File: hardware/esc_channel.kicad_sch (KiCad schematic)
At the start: 39 parts, among them Q3 DOY180N03T, Q4 DOY180N03T, Q5 DOY180N03T, Q6 DOY180N03T, Q7 DOY180N03T, Q8 DOY180N03T, U13 AT32F421G8U7, U14 NSG2065Q

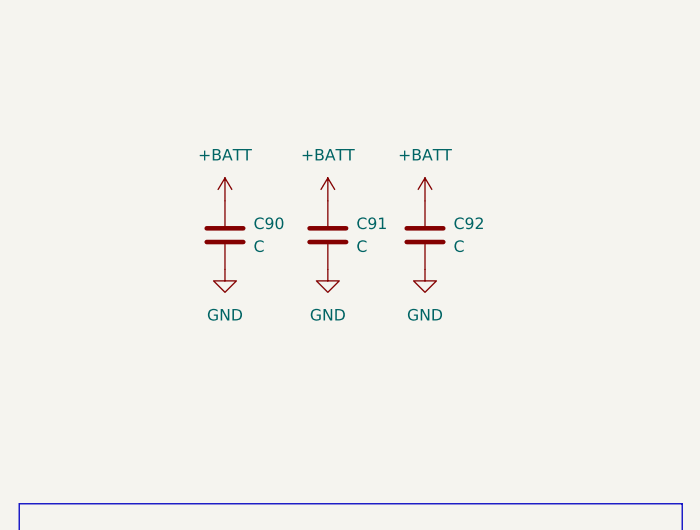
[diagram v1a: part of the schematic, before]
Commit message: Circuit: B3 bulk caps and ESP32-C3FH4, LDO caps, BMI270 aux pins, BOOTSEL 1k, unused pads
CIRCUIT_REVIEW B3, S2, S4, S5 and decision D9; LAYOUT_REVIEW 5.3 (pure
clean-up). Values and parts from hardware/KiCad-Library/PARTS-USED.md.

- B3: the 16 +BATT bulk caps had value "C" and no part. C90-C103 (0805)
  4.7uF 50V X5R CL21A475KBQNNNE (C98192, already C18/C19); C105/C106 (1206)
  4.7uF 50V X7R TCC1206X7R475K500HT (C380366, OpenESC).
- D9/B3: U22 is ESP32-C3FH4 (C2858491, in-package flash), as its NC SPI pins
  require; its in-package-flash pads 19, 21-24 deleted per instance (20 was
  already gone). L4 MPN MLZ2012M150WT000 (TDK, SX1281 reference BOM, LCSC not
  in the catalogue); D9 MPN/manufacturer/LCSC from the catalogue.
- S2, LP5912 windows (CIN > 0.5 uF effective, COUT 0.7-10 uF): U7 COUT C28
  22uF -> 1uF CL05A105KA5NQNC; U6 COUT C27 22uF -> 4.7uF CL05A475MP5NRNC;
  U7 CIN C26 100nF -> 1uF GRM033R61A105ME44D in the existing 0201 (an 0402
  does not fit beside U7 without moving parts; ~0.5 uF effective at 4.6 V,
  so it is marginal until U7 moves to the Core in R2, decision S1).
- S4: BMI270 U8 ASDx/ASCx (pins 2/3) were on GND, which the datasheet
  forbids; now +3.3V (VDDIO), valid for the LSM6DSV16X option too.
  Schematic: the GND drop replaced by a +3.3V symbol. Core: pads 2/3 and the
  via between them re-netted, 0.15 mm In3 stub to the In3 +3.3V pour.
- S5: BOOTSEL resistor R7 10k -> 1k (0201WMF1001TEE, C270365): 10k with the
  32k minimum pull-up gave 0.79 V against VIL 0.8 V.
- LAYOUT_REVIEW 5.3, pads on no net with nothing attached: U13/U15/U17/U19
  (AT32F421) 3, 8, 9, 12, 23, 24, 26-28; U14/U16/U18/U20 (NSG2065Q) NC 5, 7,
  8, 21; U7 NC 2; U21 6 (XTB, TCXO), 9, 10 (DIO2/3); Core U2 55-59 (QSPI,
  in-package flash). 60 pads in all; U8 kept for joint symmetry. AT32
  firmware must keep the dropped pins as outputs or pulled.
- Footprint values and fields synced from the schematic for the changed refs.

Deferred: RX LED D9 to +4v5 (S10). +4v5 copper is 1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
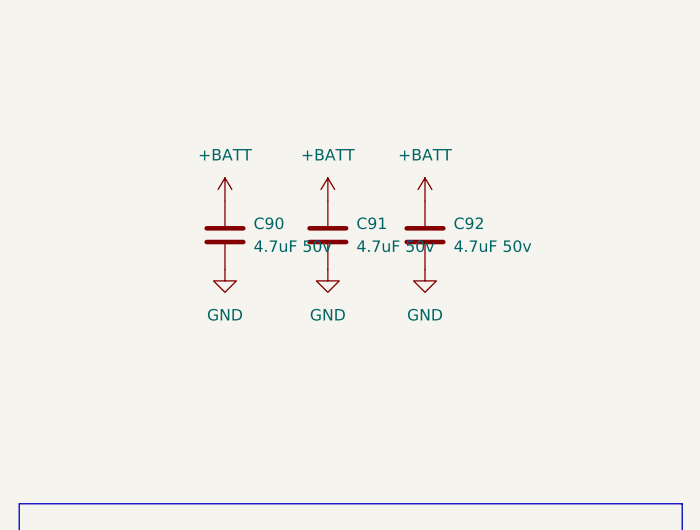
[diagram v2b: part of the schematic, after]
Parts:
- C90, C91, C92: value C -> 4.7uF 50v; LCSC (none) -> C98192; MPN (none) -> CL21A475KBQNNNE; Manufacturer (none) -> Samsung Electro-Mechanics
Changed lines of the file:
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@@
 			)
 		)
-		(property "Value" "C"
+		(property "Value" "4.7uF 50v"
 			(at 248.92 40.6399 0)
 			(show_name no)
@@
 			)
 		)
+		(property "LCSC" "C98192"
+			(at 248.92 40.6399 0)
+			(hide yes)
+			(show_name no)
+			(do_not_autoplace no)
+			(effects
+				(font
+					(size 1.27 1.27)
+				)
+				(justify left)
+			)
+		)
+		(property "MPN" "CL21A475KBQNNNE"
+			(at 248.92 40.6399 0)
+			(hide yes)
+			(show_name no)
+			(do_not_autoplace no)
+			(effects
+				(font
+					(size 1.27 1.27)
+				)
+				(justify left)
+			)
+		)
+		(property "Manufacturer" "Samsung Electro-Mechanics"
+			(at 248.92 40.6399 0)
+			(hide yes)
+			(show_name no)
+			(do_not_autoplace no)
+			(effects
+				(font
+					(size 1.27 1.27)
+				)
+				(justify left)
+			)
+		)
 		(pin "2"
 		)
@@
 			)
 		)
-		(property "Value" "C"
+		(property "Value" "4.7uF 50v"
 			(at 238.125 40.6399 0)
 			(show_name no)
@@
 			)
 		)
+		(property "LCSC" "C98192"
+			(at 238.125 40.6399 0)
+			(hide yes)
+			(show_name no)
+			(do_not_autoplace no)
+			(effects
+				(font
+					(size 1.27 1.27)
+				)
+				(justify left)
+			)
+		)
+		(property "MPN" "CL21A475KBQNNNE"
+			(at 238.125 40.6399 0)
+			(hide yes)
+			(show_name no)
+			(do_not_autoplace no)
+			(effects
+				(font
+					(size 1.27 1.27)
+				)
+				(justify left)
+			)
+		)
+		(property "Manufacturer" "Samsung Electro-Mechanics"
+			(at 238.125 40.6399 0)
+			(hide yes)
+			(show_name no)
+			(do_not_autoplace no)
+			(effects
+				(font
+					(size 1.27 1.27)
+				)
+				(justify left)
+			)
+		)
 		(pin "2"
 		)
@@
 			)
 		)
-		(property "Value" "C"
+		(property "Value" "4.7uF 50v"
 			(at 226.695 40.6399 0)
 			(show_name no)
@@
 			)
 		)
+		(property "LCSC" "C98192"
+			(at 226.695 40.6399 0)
+			(hide yes)
+			(show_name no)
+			(do_not_autoplace no)
+			(effects
+				(font
+					(size 1.27 1.27)
+				)
+				(justify left)
+			)
+		)
+		(property "MPN" "CL21A475KBQNNNE"
+			(at 226.695 40.6399 0)
+			(hide yes)
+			(show_name no)
+			(do_not_autoplace no)
+			(effects
+				(font
+					(size 1.27 1.27)
+				)
+				(justify left)
+			)
+		)
+		(property "Manufacturer" "Samsung Electro-Mechanics"
+			(at 226.695 40.6399 0)
+			(hide yes)
+			(show_name no)
+			(do_not_autoplace no)
+			(effects
+				(font
+					(size 1.27 1.27)
+				)
+				(justify left)
+			)
+		)

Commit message: Owner rules: no component silk, pad labels and values, no wordmark text, MPN + maker on every BOM line
The owner rules adopted in PLAN.md (pcb-agent-commons, 2026-10-06), applied
where they are local edits:

- No component silkscreen. J91's reference was the only visible one (Core
  B.Silkscreen, under the LGA) and is hidden. Footprint silk graphics removed
  per instance: Base 234, Core 72. Kept: connector outlines and pin-1 marks
  (USB1, U12 SH-6, Card1, JP1) and the LGA pin-1 marks (J90, J91). Base
  lib_footprint_mismatch warnings 31 -> 40 as a result.
- Solder-pad labels: Core J53 (GND) had none, now "gnd" in the style of J52's
  label. The SH-6 per-pin labels ("10v gnd T0", "R0 gnd R1") become the port
  name "DJI" (connectors: name and pin-1 mark only). Core J48-J51 have no room:
  0.5 mm to J44 above, 0.93 mm to the board edge below. CIRCUIT_REVIEW 8.3
  moves them off the LGA in R2, so their labels go with that move.
- Pad values: all 40 solder-pad symbols said "5V". Each now carries its
  function (5V, GND, LED, BUZ+/BUZ-, 10V, 4V5, CAM, VTX, SCL, SDA, TX0/RX0,
  TX1/RX1, PIO_TX0/PIO_RX0; off-board J19 ADC2, J22 GND, J46/J47 NC).
- No "Drone" text: the "OpenDrone" wordmark on Core F.Silkscreen (9 filled
  polygons in two groups) is removed; a TODO for the incutec wordmark from the
  brand repo sits on User.Comments (not fabricated). No other such text on any
  copper, mask or silk layer of either board.
- BOM: lines missing manufacturer or MPN 41 -> 1. MPNs come from
  PARTS-USED.md by LCSC number. Manufacturers come from the catalogue symbol,
  this design's spelling for the same MPN family, or the committed datasheet
  (NSIC, Sofng, Jiangsu Changjing, Hirose). Still open: Rsense2
  ASR-S-3-0.2F (C695806), whose manufacturer nothing in the catalogue states.
  U24 (board outline) and TP9 (BOOT solder pad) are not parts: excluded from
  BOM and position files.
- 0201 default / minimal capacitance: respected in the circuit commit (C26
  stays 0201; no belt-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
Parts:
- C37, C38, C39, C43: Manufacturer (none) -> Murata Electronics
- C40, C41, C42: Manufacturer (none) -> Samsung Electro-Mechanics
- Q3, Q4, Q5, Q6, Q7, Q8: Manufacturer (none) -> DOINGTER
- R35, R36, R41, R42, R43, R44, R46, R49, R52: Manufacturer (none) -> UNI-ROYAL
- R37, R38, R39, R40, R45, R47, R48, R50, R51, R53: Manufacturer (none) -> YAGEO
- U14: Manufacturer (none) -> NSIC
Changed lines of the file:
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@@
 			)
 		)
-		(property "Manufacturer" ""
+		(property "Manufacturer" "YAGEO"
 			(at 0 0 0)
 			(hide yes)
@@
 			)
 		)
-		(property "Manufacturer" ""
+		(property "Manufacturer" "UNI-ROYAL"
 			(at 0 0 0)
 			(hide yes)
@@
 			)
 		)
-		(property "Manufacturer" ""
+		(property "Manufacturer" "Murata Electronics"
 			(at 0 0 0)
 			(hide yes)
@@
 			)
 		)
-		(property "Manufacturer" ""
+		(property "Manufacturer" "UNI-ROYAL"
 			(at 0 0 0)
 			(hide yes)
@@
 			)
 		)
-		(property "Manufacturer" ""
+		(property "Manufacturer" "Samsung Electro-Mechanics"
 			(at 0 0 0)
 			(hide yes)
@@
 			)
 		)
-		(property "Manufacturer" ""
+		(property "Manufacturer" "NSIC"
 			(at 0 0 0)
 			(hide yes)
@@
 			)
 		)
-		(property "Manufacturer" ""
+		(property "Manufacturer" "YAGEO"
 			(at 0 0 0)
 			(hide yes)
@@
 			)
 		)
-		(property "Manufacturer" ""
+		(property "Manufacturer" "YAGEO"
 			(at 0 0 0)
 			(hide yes)
@@
 			)
 		)
-		(property "Manufacturer" ""
+		(property "Manufacturer" "Murata Electronics"
 			(at 0 0 0)
 			(hide yes)
@@
 			)
 		)
-		(property "Manufacturer" ""
+		(property "Manufacturer" "YAGEO"
 			(at 0 0 0)
 			(hide yes)
@@
 			)
 		)
-		(property "Manufacturer" ""
+		(property "Manufacturer" "YAGEO"
 			(at 0 0 0)
 			(hide yes)
@@
 			)
 		)
-		(property "Manufacturer" ""
+		(property "Manufacturer" "Murata Electronics"
 			(at 0 0 0)
 			(hide yes)
@@
 			)
 		)
-		(property "Manufacturer" ""
+		(property "Manufacturer" "UNI-ROYAL"
 			(at 0 0 0)
 			(hide yes)
@@
 			)
 		)
-		(property "Manufacturer" ""
+		(property "Manufacturer" "YAGEO"
 			(at 0 0 0)
 			(hide yes)
@@
 			)
 		)
-		(property "Manufacturer" ""
+		(property "Manufacturer" "Samsung Electro-Mechanics"
 			(at 0 0 0)
 			(hide yes)
@@
 			)
 		)
-		(property "Manufacturer" ""
+		(property "Manufacturer" "YAGEO"
 			(at 0 0 0)
 			(hide yes)
@@
 			)
 		)
-		(property "Manufacturer" ""
+		(property "Manufacturer" "UNI-ROYAL"
 			(at 0 0 0)
 			(hide yes)
@@
 			)
 		)
-		(property "Manufacturer" ""
+		(property "Manufacturer" "Murata Electronics"
 			(at 0 0 0)
 			(hide yes)
@@
 			)
 		)
-		(property "Manufacturer" ""
+		(property "Manufacturer" "UNI-ROYAL"
 			(at 0 0 0)
 			(hide yes)
@@
 			)
 		)
-		(property "Manufacturer" ""
+		(property "Manufacturer" "DOINGTER"
 			(at 0 0 0)
 			(hide yes)
@@
 			)
 		)
-		(property "Manufacturer" ""
+		(property "Manufacturer" "UNI-ROYAL"
 			(at 0 0 0)
 			(hide yes)
@@
 			)
 		)
-		(property "Manufacturer" ""
+		(property "Manufacturer" "UNI-ROYAL"
 			(at 0 0 0)
 			(hide yes)
@@
 			)
 		)
-		(property "Manufacturer" ""
+		(property "Manufacturer" "DOINGTER"
 			(at 0 0 0)
 			(hide yes)
@@
 			)
 		)
-		(property "Manufacturer" ""
+		(property "Manufacturer" "UNI-ROYAL"
 			(at 0 0 0)
 			(hide yes)
@@
 			)
 		)
-		(property "Manufacturer" ""
+		(property "Manufacturer" "DOINGTER"
 			(at 0 0 0)
 			(hide yes)
@@
 			)
 		)
-		(property "Manufacturer" ""
+		(property "Manufacturer" "UNI-ROYAL"
 			(at 0 0 0)
 			(hide yes)
@@
 			)
 		)
-		(property "Manufacturer" ""
+		(property "Manufacturer" "Samsung Electro-Mechanics"
 			(at 0 0 0)
 			(hide yes)
@@
 			)
 		)
-		(property "Manufacturer" ""
+		(property "Manufacturer" "YAGEO"
 			(at 0 0 0)
 			(hide yes)
@@
 			)
 		)
-		(property "Manufacturer" ""
+		(property "Manufacturer" "DOINGTER"
 			(at 0 0 0)
 			(hide yes)
@@
 			)
 		)
-		(property "Manufacturer" ""
+		(property "Manufacturer" "YAGEO"
 			(at 0 0 0)
 			(hide yes)
@@
 			)
 		)
-		(property "Manufacturer" ""
+		(property "Manufacturer" "YAGEO"
 			(at 0 0 0)
 			(hide yes)
@@
 			)
 		)
-		(property "Manufacturer" ""
+		(property "Manufacturer" "DOINGTER"
 			(at 0 0 0)
 			(hide yes)
@@
 			)
 		)
-		(property "Manufacturer" ""
+		(property "Manufacturer" "DOINGTER"
 			(at 0 0 0)
 			(hide yes)

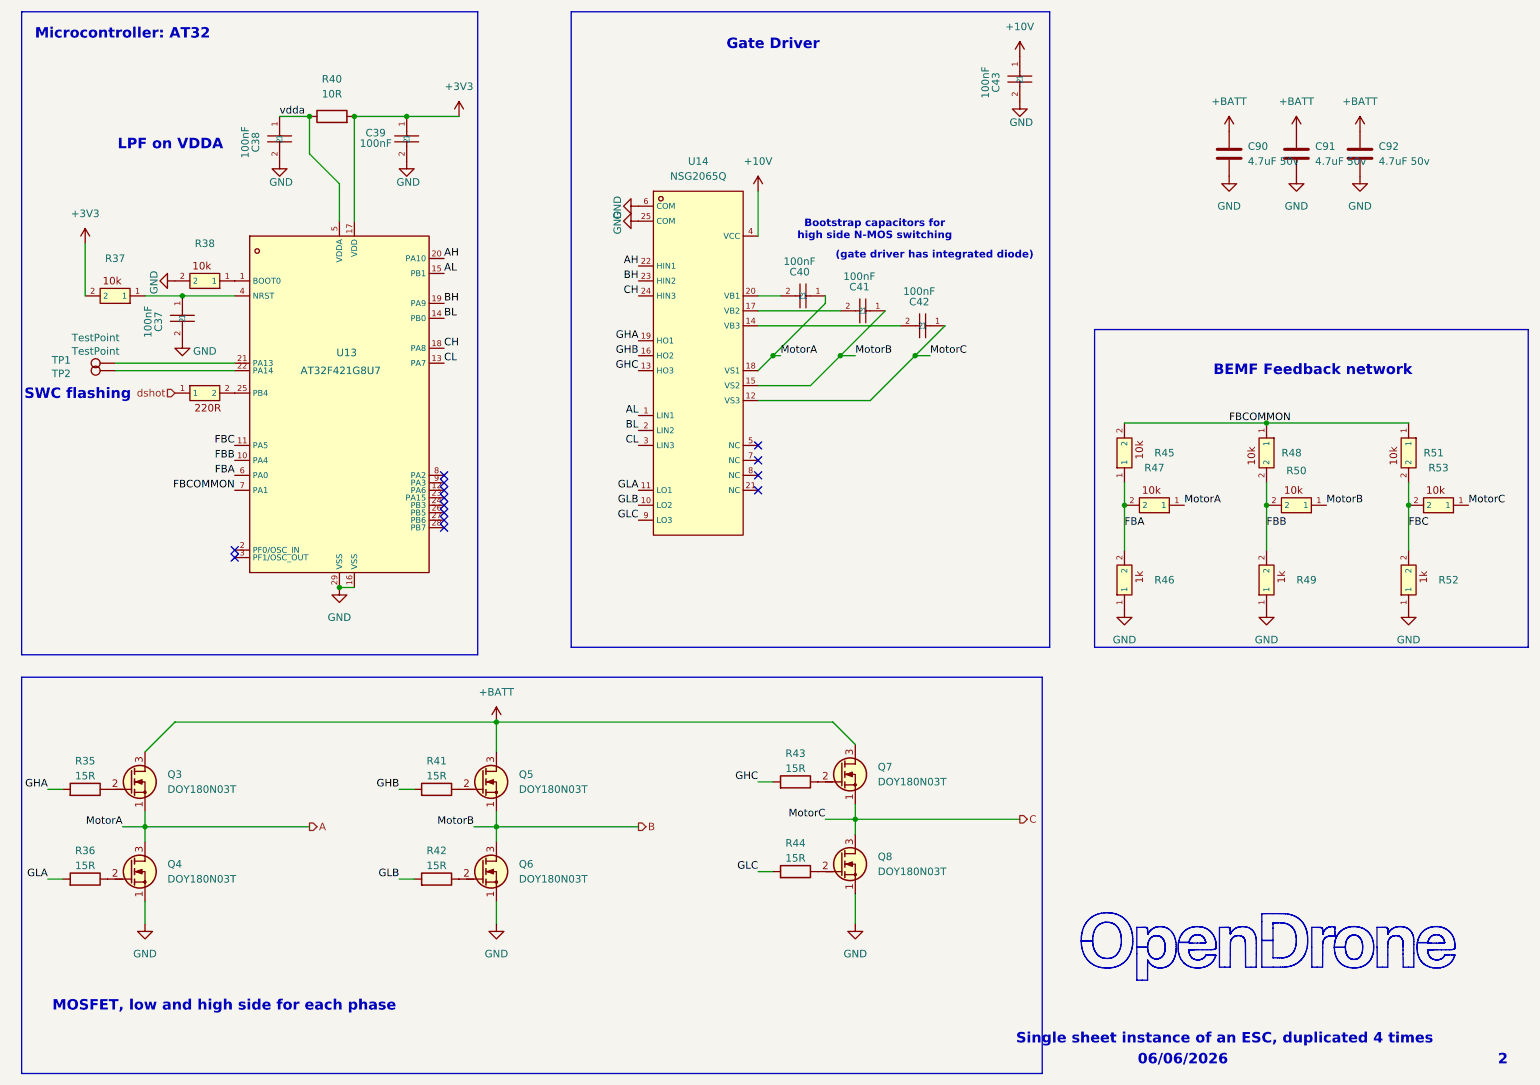
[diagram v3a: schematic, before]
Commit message: DFM: DOY180N03T land from the datasheet package, EP keepout (24 FETs)
DFM-03 compromise (FET-stack offset decision pending, via arrays kept).

New project footprint lib:DOY180N03T_TDFN3333-8. The S/G pads, drain
fingers and paste stay as in KiCad PowerDI3333-8. The drain land goes
from x -0.40..1.31 to -0.415..1.35 (fp-local, source side -x). That is
the largest common extension. The HS/LS via arrays of the stacked pairs
sit inside the datasheet EP outline (2.15 x 2.75 mm, DOY180N03T.pdf
p.6): 64 GND + 11 gate vias under the HS EPs, and 22 GND vias, 11 gate
vias and 25 GND track pieces under the LS EPs. The closest are 0.155 mm
from the stock land (rule 0.14). Growing the land 0.03 mm in y already
conflicts on 16 FETs. EP coverage goes from 69.2 % to 70.3 % on all 24.

Rule area DOY_EP (EP outline, pad layer) in the footprint, plus two
Base DRU rules: other-net pours stay 0.40 mm from the drain land, and no
track or via of a net other than GND/+BATT/gate/phase may enter DOY_EP
(A.NetName; A.Net does not match names). A footprint pour keepout was
tried first. KiCad keepouts are not net-aware, so it cut the +BATT
drain pour (+BATT 0.584 -> 0.641 mOhm). A track/via keepout would flag
the 133 via-array items.

Foreign copper under the uncovered EP: pours 4.70 -> 0.26 mm2 (only EP
corner specks, max 0.033 mm2 per FET; 0.53 mm removes them but costs
GND +0.006 mOhm). Vias (3.52 mm2) and tracks (3.58 mm2) are unchanged:
they are the via arrays.

All 24 swapped in place: same position, rotation, side, nets, fields
and paths; pad position error 0. Schematic: Footprint field of the 6 Q
symbols in esc_channel.kicad_sch (4 instances) set with kicad-skip,
then `kicad-cli sch upgrade --force`. In this 4-instance sheet the
upgrade also sets the default Reference text of 64 symbols to another
instance's reference. A plain upgrade of the unchanged sheet does the
same, and the instance references are untouched.

DC (lr_power method, h 0.05): +BATT 0.584 -> 0.584, GND 0.358 -> 0.359,
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
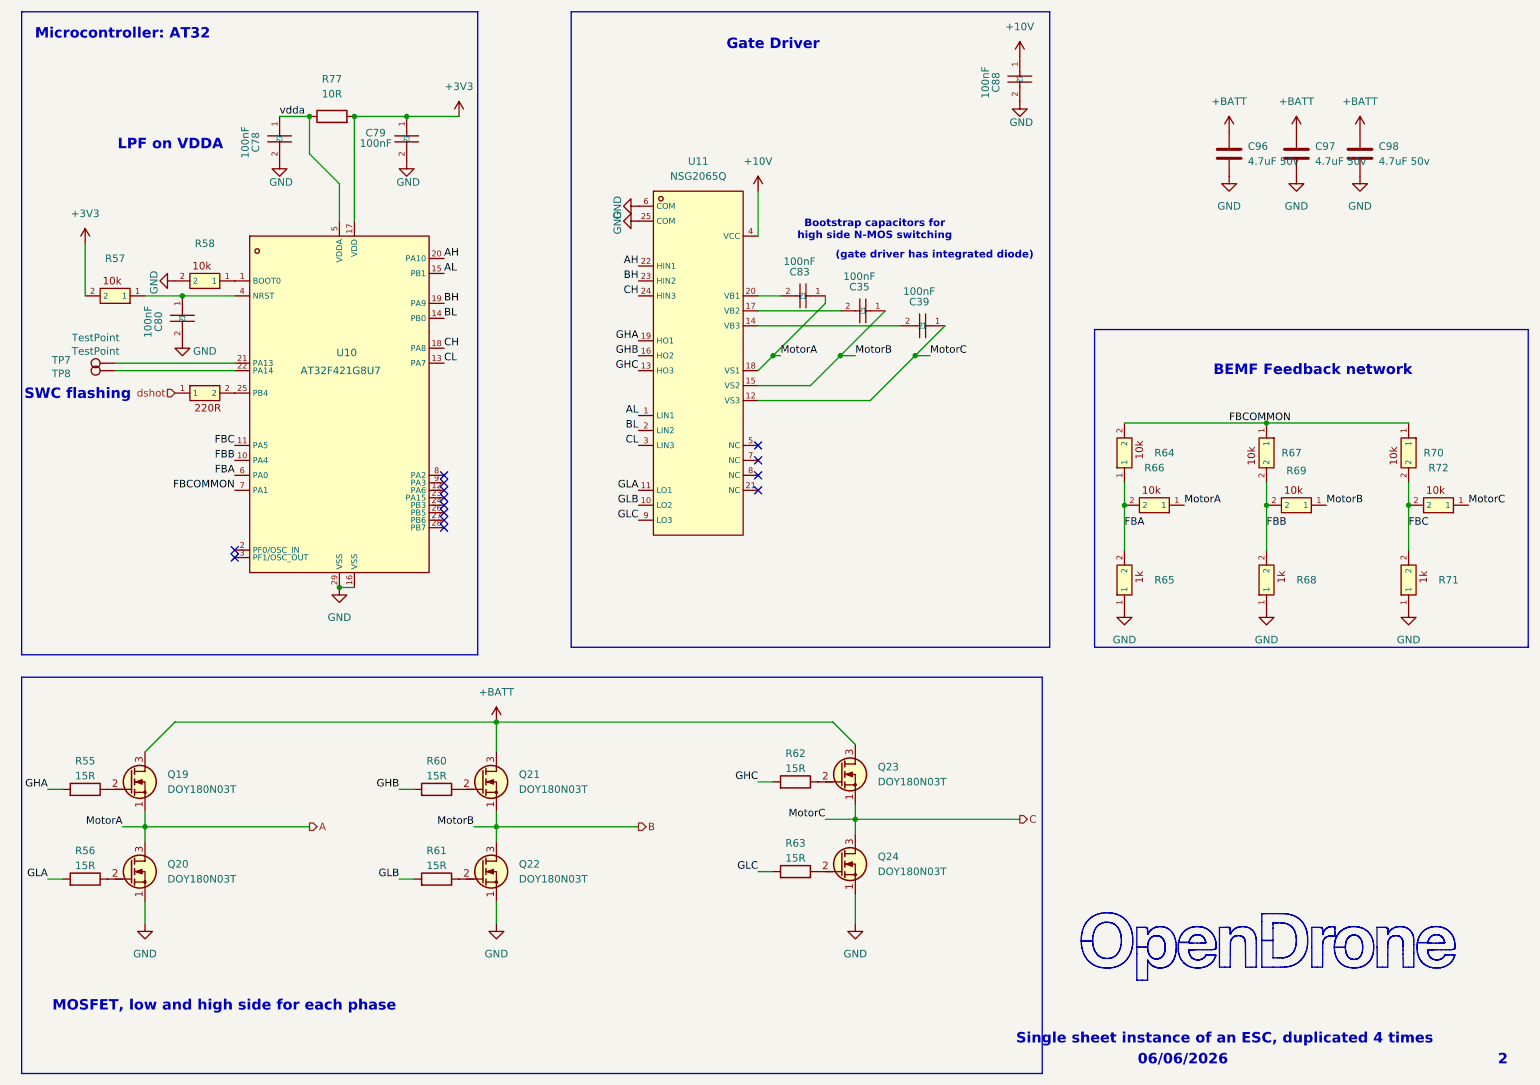
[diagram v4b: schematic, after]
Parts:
- Q19: renamed from Q3; footprint Package_SON:Diodes_PowerDI3333-8 -> lib:DOY180N03T_TDFN3333-8
- Q20: renamed from Q4; footprint Package_SON:Diodes_PowerDI3333-8 -> lib:DOY180N03T_TDFN3333-8
- Q21: renamed from Q5; footprint Package_SON:Diodes_PowerDI3333-8 -> lib:DOY180N03T_TDFN3333-8
- Q22: renamed from Q6; footprint Package_SON:Diodes_PowerDI3333-8 -> lib:DOY180N03T_TDFN3333-8
- Q23: renamed from Q7; footprint Package_SON:Diodes_PowerDI3333-8 -> lib:DOY180N03T_TDFN3333-8
- Q24: renamed from Q8; footprint Package_SON:Diodes_PowerDI3333-8 -> lib:DOY180N03T_TDFN3333-8
- renumbered C41 to C35, C42 to C39, C38 to C78, C39 to C79, C37 to C80, C40 to C83, C43 to C88, C90 to C96, C91 to C97, C92 to C98, R35 to R55, R36 to R56, R37 to R57, R38 to R58, R39 to R59, R41 to R60, R42 to R61, R43 to R62, R44 to R63, R45 to R64, R46 to R65, R47 to R66, R48 to R67, R49 to R68, R50 to R69, R51 to R70, R52 to R71, R53 to R72, R40 to R77, TP1 to TP7, TP2 to TP8, U13 to U10, U14 to U11
